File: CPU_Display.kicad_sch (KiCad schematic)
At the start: 1 part

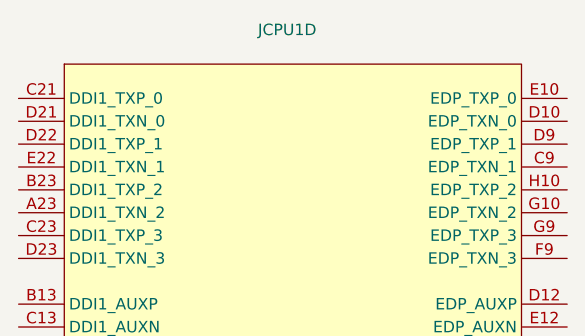
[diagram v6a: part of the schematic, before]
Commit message: Added first PCH symbol and footprint
THANKS @mothenjoyer69 so much for extracting and converting the PCH footprint from a laptop boardview ❤️
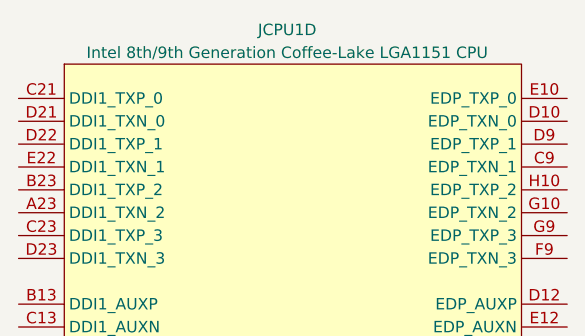
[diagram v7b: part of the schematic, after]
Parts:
- JCPU1: value ~ -> Intel 8th/9th Generation Coffee-Lake LGA1151 CPU

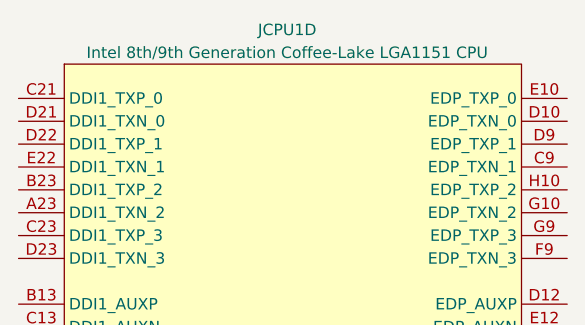
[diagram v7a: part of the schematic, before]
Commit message: Added all the PCH symbols
that took 1.5 days straight lol
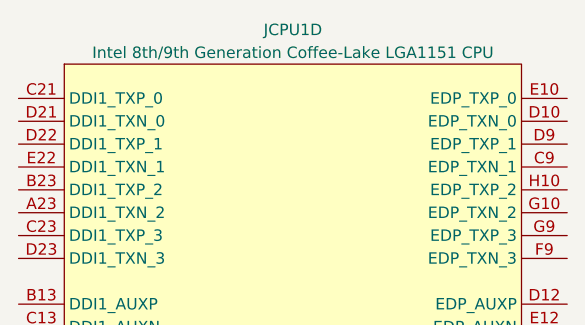
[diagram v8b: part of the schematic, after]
